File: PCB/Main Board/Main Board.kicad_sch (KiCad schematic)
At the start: 4 parts

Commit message: quality of life changes plus wiring plus buffering plus value changes
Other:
- sheet Auto-Balancing Bridge ports: added AC_100, AC_10k, AC_1k, AC_EN, IBmonitor, OUT+, OUT-, R_SEL_10, R_SEL_100, R_SEL_100k, R_SEL_10k, R_SEL_1k, R_SEL_432k; removed none
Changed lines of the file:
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@@
+	(wire
+		(pts
+			(xy 139.7 133.35) (xy 190.5 133.35)
+		)
+		(stroke
+			(width 0)
+			(type default)
+		)
+	)
+	(wire
+		(pts
+			(xy 139.7 156.21) (xy 190.5 156.21)
+		)
+		(stroke
+			(width 0)
+			(type default)
+		)
+	)
 	(wire
 		(pts
@@
 	(wire
 		(pts
+			(xy 139.7 140.97) (xy 190.5 140.97)
+		)
+		(stroke
+			(width 0)
+			(type default)
+		)
+	)
+	(wire
+		(pts
 			(xy 139.7 78.74) (xy 152.4 78.74)
 		)
@@
 	(wire
 		(pts
+			(xy 139.7 151.13) (xy 190.5 151.13)
+		)
+		(stroke
+			(width 0)
+			(type default)
+		)
+	)
+	(wire
+		(pts
 			(xy 139.7 45.72) (xy 152.4 45.72)
 		)
@@
 	(wire
 		(pts
+			(xy 139.7 130.81) (xy 190.5 130.81)
+		)
+		(stroke
+			(width 0)
+			(type default)
+		)
+	)
+	(wire
+		(pts
+			(xy 139.7 148.59) (xy 190.5 148.59)
+		)
+		(stroke
+			(width 0)
+			(type default)
+		)
+	)
+	(wire
+		(pts
 			(xy 215.9 114.3) (xy 248.92 114.3)
 		)
@@
 	(wire
 		(pts
+			(xy 139.7 153.67) (xy 190.5 153.67)
+		)
+		(stroke
+			(width 0)
+			(type default)
+		)
+	)
+	(wire
+		(pts
 			(xy 139.7 35.56) (xy 152.4 35.56)
 		)
@@
 	(wire
 		(pts
+			(xy 139.7 146.05) (xy 190.5 146.05)
+		)
+		(stroke
+			(width 0)
+			(type default)
+		)
+	)
+	(wire
+		(pts
 			(xy 139.7 86.36) (xy 152.4 86.36)
 		)
@@
 	(wire
 		(pts
+			(xy 139.7 138.43) (xy 190.5 138.43)
+		)
+		(stroke
+			(width 0)
+			(type default)
+		)
+	)
+	(wire
+		(pts
+			(xy 139.7 143.51) (xy 190.5 143.51)
+		)
+		(stroke
+			(width 0)
+			(type default)
+		)
+	)
+	(wire
+		(pts
 			(xy 139.7 114.3) (xy 152.4 114.3)
+		)
+		(stroke
+			(width 0)
+			(type default)
+		)
+	)
+	(wire
+		(pts
+			(xy 139.7 135.89) (xy 190.5 135.89)
 		)
 		(stroke
@@
 	(sheet
 		(at 190.5 101.6)
-		(size 25.4 25.4)
+		(size 25.4 58.42)
 		(exclude_from_sim no)
 		(in_bom yes)
@@
 		)
 		(property "Sheetfile" "Bridge.kicad_sch"
-			(at 190.5 127.5846 0)
+			(at 190.5 160.6046 0)
 			(effects
 				(font
@@
 		(pin "Out-" output
 			(at 190.5 116.84 180)
+			(effects
+				(font
+					(size 1.27 1.27)
+				)
+				(justify left)
+			)
+		)
+		(pin "AC_EN" input
+			(at 190.5 133.35 180)
+			(effects
+				(font
+					(size 1.27 1.27)
+				)
+				(justify left)
+			)
+		)
+		(pin "OUT-" output
+			(at 190.5 119.38 180)
+			(effects
+				(font
+					(size 1.27 1.27)
+				)
+				(justify left)
+			)
+		)
+		(pin "OUT+" output
+			(at 190.5 114.3 180)
+			(effects
+				(font
+					(size 1.27 1.27)
+				)
+				(justify left)
+			)
+		)
+		(pin "AC_100" input
+			(at 190.5 138.43 180)
+			(effects
+				(font
+					(size 1.27 1.27)
+				)
+				(justify left)
+			)
+		)
+		(pin "IBmonitor" output
+			(at 190.5 130.81 180)
+			(effects
+				(font
+					(size 1.27 1.27)
+				)
+				(justify left)
+			)
+		)
+		(pin "AC_1k" input
+			(at 190.5 135.89 180)
+			(effects
+				(font
+					(size 1.27 1.27)
+				)
+				(justify left)
+			)
+		)
+		(pin "AC_10k" input
+			(at 190.5 140.97 180)
+			(effects
+				(font
+					(size 1.27 1.27)
+				)
+				(justify left)
+			)
+		)
+		(pin "R_SEL_100" input
+			(at 190.5 146.05 180)
+			(effects
+				(font
+					(size 1.27 1.27)
+				)
+				(justify left)
+			)
+		)
+		(pin "R_SEL_10" input
+			(at 190.5 143.51 180)
+			(effects
+				(font
+					(size 1.27 1.27)
+				)
+				(justify left)
+			)
+		)
+		(pin "R_SEL_432k" input
+			(at 190.5 156.21 180)
+			(effects
+				(font
+					(size 1.27 1.27)
+				)
+				(justify left)
+			)
+		)
+		(pin "R_SEL_10k" input
+			(at 190.5 148.59 180)
+			(effects
+				(font
+					(size 1.27 1.27)
+				)
+				(justify left)
+			)
+		)
+		(pin "R_SEL_100k" input
+			(at 190.5 153.67 180)
+			(effects
+				(font
+					(size 1.27 1.27)
+				)
+				(justify left)
+			)
+		)
+		(pin "R_SEL_1k" input
+			(at 190.5 151.13 180)
 			(effects
 				(font
@@
 	(sheet
 		(at 114.3 25.4)
-		(size 25.4 101.6)
+		(size 25.4 134.62)
 		(exclude_from_sim no)
 		(in_bom yes)
@@
 		)
 		(property "Sheetfile" "Processor.kicad_sch"
-			(at 114.3 127.5846 0)
-			(effects
-				(font
+			(at 114.3 160.6046 0)
+			(effects
+				(font

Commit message: footprints and minor
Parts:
- gave numbers to parts that had none: 4
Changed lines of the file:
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@@
 		(dnp no)
 		(fields_autoplaced yes)
-		(property "Reference" "J?"
+		(property "Reference" "J4"
 			(at 257.81 113.3231 0)
 			(effects
@@
 			(project "Main Board"
 				(path "/20aae4b7-3fb8-4924-82e8-1e7a29a313f8"
-					(reference "J?")
+					(reference "J4")
 					(unit 1)
 				)
@@
 		(dnp no)
 		(fields_autoplaced yes)
-		(property "Reference" "J?"
+		(property "Reference" "J2"
 			(at 257.81 62.5231 0)
 			(effects
@@
 			(project "Main Board"
 				(path "/20aae4b7-3fb8-4924-82e8-1e7a29a313f8"
-					(reference "J?")
+					(reference "J2")
 					(unit 1)
 				)
@@
 		(dnp no)
 		(fields_autoplaced yes)
-		(property "Reference" "J?"
+		(property "Reference" "J3"
 			(at 257.81 87.9231 0)
 			(effects
@@
 			(project "Main Board"
 				(path "/20aae4b7-3fb8-4924-82e8-1e7a29a313f8"
-					(reference "J?")
+					(reference "J3")
 					(unit 1)
 				)
@@
 		(dnp no)
 		(fields_autoplaced yes)
-		(property "Reference" "J?"
+		(property "Reference" "J1"
 			(at 257.81 37.1231 0)
 			(effects
@@
 			(project ""
 				(path "/20aae4b7-3fb8-4924-82e8-1e7a29a313f8"
-					(reference "J?")
-					(unit 1)
-				)
+					(reference "J1")
+					(unit 1)
+				)

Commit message: footprints and stm wiring
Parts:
- J1, J2, J3, J4: footprint (none) -> Connector_Coaxial:BNC_TEConnectivity_1478035_Horizontal
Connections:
- net Guard_{out} is gone; now on net GUARD: J3.2 (Ext), J4.2 (Ext)
- net GUARD: now reaches J2.2 (Ext)
- net GUARD: now also J1.2 (Ext)
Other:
- sheet Auto-Balancing Bridge ports: added DC_INT_ISO, I_B_MONITOR; removed IBmonitor, Out+, Out-
- sheet Current Amplifier: file Amplifier.kicad_sch -> currentamp.kicad_sch
- sheet Processor ports: added DC_INT_ISO, R_SEL_10, R_SEL_100, R_SEL_10k, R_SEL_1k, SIG_SOURCE; removed none
- sheet Signal Source ports: added SIG_SOURCE; removed none
- sheet Voltage Amplifier: file Amplifier.kicad_sch -> voltageamp.kicad_sch

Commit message: relays and layout begin
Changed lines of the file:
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@@
 	)
 	(sheet
-		(at 77.47 134.62)
+		(at 76.2 135.89)
 		(size 25.4 25.4)
 		(exclude_from_sim no)
@@
 		)
 		(property "Sheetname" "Power"
-			(at 77.47 133.9084 0)
+			(at 76.2 135.1784 0)
 			(effects
 				(font
@@
 		)
 		(property "Sheetfile" "Power.kicad_sch"
-			(at 77.47 160.6046 0)
+			(at 76.2 161.8746 0)
 			(effects
 				(font

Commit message: minor and layout
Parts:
- added H1, H2, H3, H4: MountingHole, MountingHole:MountingHole_3.2mm_M3, symbol Mechanical:MountingHole
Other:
- sheet Auto-Balancing Bridge ports: added none; removed R_SEL_432k
- moved on the sheet: J1, J2, J3, J4

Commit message: :ghost:
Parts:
- renumbered H1 to H101, H2 to H102, H3 to H103, H4 to H104, J1 to J101, J2 to J102, J3 to J103, J4 to J104
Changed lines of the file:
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@@
 		(dnp no)
 		(fields_autoplaced yes)
-		(property "Reference" "H4"
+		(property "Reference" "H104"
 			(at 38.1 149.8599 0)
 			(effects
@@
 			(project "Main Board"
 				(path "/20aae4b7-3fb8-4924-82e8-1e7a29a313f8"
-					(reference "H4")
+					(reference "H104")
 					(unit 1)
 				)
@@
 		(dnp no)
 		(fields_autoplaced yes)
-		(property "Reference" "H3"
+		(property "Reference" "H103"
 			(at 38.1 144.7799 0)
 			(effects
@@
 			(project "Main Board"
 				(path "/20aae4b7-3fb8-4924-82e8-1e7a29a313f8"
-					(reference "H3")
+					(reference "H103")
 					(unit 1)
 				)
@@
 		(dnp no)
 		(fields_autoplaced yes)
-		(property "Reference" "J4"
+		(property "Reference" "J104"
 			(at 233.68 110.7831 0)
 			(effects
@@
 			(project "Main Board"
 				(path "/20aae4b7-3fb8-4924-82e8-1e7a29a313f8"
-					(reference "J4")
+					(reference "J104")
 					(unit 1)
 				)
@@
 		(dnp no)
 		(fields_autoplaced yes)
-		(property "Reference" "J2"
+		(property "Reference" "J102"
 			(at 233.68 59.9831 0)
 			(effects
@@
 			(project "Main Board"
 				(path "/20aae4b7-3fb8-4924-82e8-1e7a29a313f8"
-					(reference "J2")
+					(reference "J102")
 					(unit 1)
 				)
@@
 		(dnp no)
 		(fields_autoplaced yes)
-		(property "Reference" "H2"
+		(property "Reference" "H102"
 			(at 38.1 139.6999 0)
 			(effects
@@
 			(project "Main Board"
 				(path "/20aae4b7-3fb8-4924-82e8-1e7a29a313f8"
-					(reference "H2")
+					(reference "H102")
 					(unit 1)
 				)
@@
 		(dnp no)
 		(fields_autoplaced yes)
-		(property "Reference" "J3"
+		(property "Reference" "J103"
 			(at 233.68 85.3831 0)
 			(effects
@@
 			(project "Main Board"
 				(path "/20aae4b7-3fb8-4924-82e8-1e7a29a313f8"
-					(reference "J3")
+					(reference "J103")
 					(unit 1)
 				)
@@
 		(dnp no)
 		(fields_autoplaced yes)
-		(property "Reference" "H1"
+		(property "Reference" "H101"
 			(at 38.1 134.6199 0)
 			(effects
@@
 			(project ""
 				(path "/20aae4b7-3fb8-4924-82e8-1e7a29a313f8"
-					(reference "H1")
+					(reference "H101")
 					(unit 1)
 				)
@@
 		(dnp no)
 		(fields_autoplaced yes)
-		(property "Reference" "J1"
+		(property "Reference" "J101"
 			(at 233.68 34.5831 0)
 			(effects
@@
 			(project ""
 				(path "/20aae4b7-3fb8-4924-82e8-1e7a29a313f8"
-					(reference "J1")
-					(unit 1)
-				)
+					(reference "J101")
+					(unit 1)
+				)

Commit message: Layout progress
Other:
- sheet Processor ports: added IAmp.Out, VAmp.Out; removed IAmp.In, VAmp.In
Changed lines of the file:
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@@
 			)
 		)
-		(pin "VAmp.In" input
+		(pin "VAmp.Out" input
 			(at 115.57 73.66 0)
 			(effects
@@
 			)
 		)
-		(pin "IAmp.In" input
+		(pin "IAmp.Out" input
 			(at 115.57 111.76 0)
 			(effects

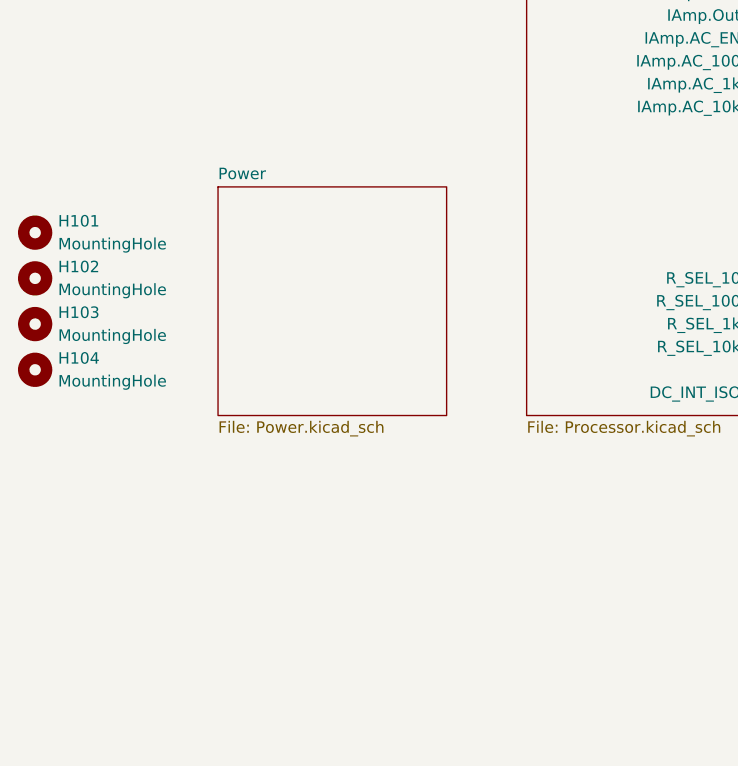
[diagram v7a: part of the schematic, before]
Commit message: transistor tester
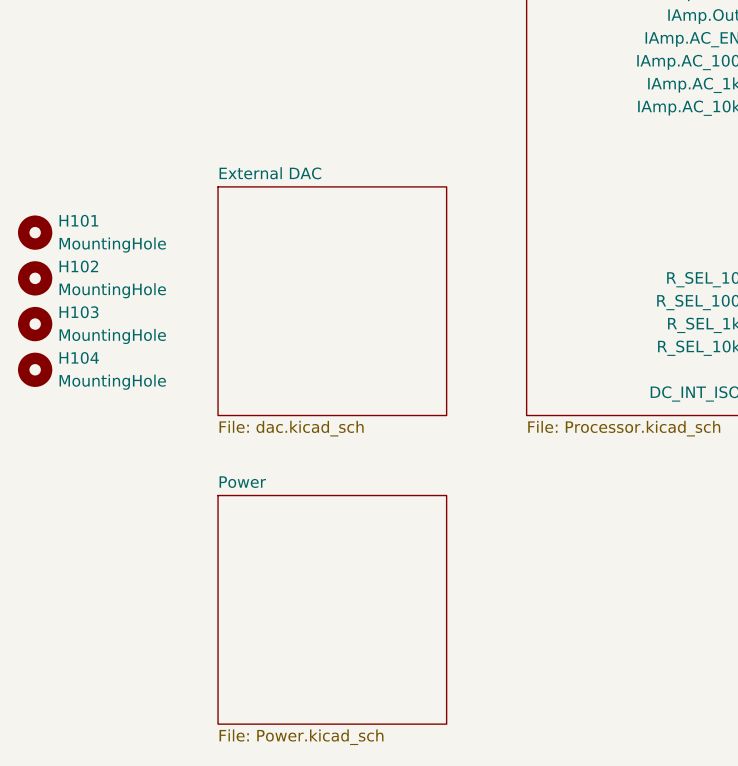
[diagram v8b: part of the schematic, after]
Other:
- added sheet External DAC (dac.kicad_sch)
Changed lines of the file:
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@@
+	)
+	(sheet
+		(at 55.88 165.1)
+		(size 25.4 25.4)
+		(exclude_from_sim no)
+		(in_bom yes)
+		(on_board yes)
+		(dnp no)
+		(fields_autoplaced yes)
+		(stroke
+			(width 0.1524)
+			(type solid)
+		)
+		(fill
+			(color 0 0 0 0.0000)
+		)
+		(property "Sheetname" "Power"
+			(at 55.88 164.3884 0)
+			(effects
+				(font
+					(size 1.27 1.27)
+				)
+				(justify left bottom)
+			)
+		)
+		(property "Sheetfile" "Power.kicad_sch"
+			(at 55.88 191.0846 0)
+			(effects
+				(font
+					(size 1.27 1.27)
+				)
+				(justify left top)
+			)
+		)
+		(instances
+			(project "Main Board"
+				(path "/20aae4b7-3fb8-4924-82e8-1e7a29a313f8"
+					(page "13")
+				)
+			)
+		)
+	)
+	(sheet
+		(at 128.27 99.06)
+		(size 25.4 25.4)
+		(exclude_from_sim no)
+		(in_bom yes)
+		(on_board yes)
+		(dnp no)
+		(fields_autoplaced yes)
+		(stroke
+			(width 0.1524)
+			(type solid)
+		)
+		(fill
+			(color 0 0 0 0.0000)
+		)
+		(property "Sheetname" "Current Amplifier"
+			(at 128.27 98.3484 0)
+			(effects
+				(font
+					(size 1.27 1.27)
+				)
+				(justify left bottom)
+			)
+		)
+		(property "Sheetfile" "currentamp.kicad_sch"
+			(at 128.27 125.0446 0)
+			(effects
+				(font
+					(size 1.27 1.27)
+				)
+				(justify left top)
+			)
+		)
+		(pin "AC_100" input
+			(at 128.27 116.84 180)
+			(effects
+				(font
+					(size 1.27 1.27)
+				)
+				(justify left)
+			)
+		)
+		(pin "AC_EN" input
+			(at 128.27 114.3 180)
+			(effects
+				(font
+					(size 1.27 1.27)
+				)
+				(justify left)
+			)
+		)
+		(pin "x3" input
+			(at 128.27 106.68 180)
+			(effects
+				(font
+					(size 1.27 1.27)
+				)
+				(justify left)
+			)
+		)
+		(pin "{slash}4" input
+			(at 128.27 101.6 180)
+			(effects
+				(font
+					(size 1.27 1.27)
+				)
+				(justify left)
+			)
+		)
+		(pin "In-" input
+			(at 153.67 114.3 0)
+			(effects
+				(font
+					(size 1.27 1.27)
+				)
+				(justify right)
+			)
+		)
+		(pin "AC_1k" input
+			(at 128.27 119.38 180)
+			(effects
+				(font
+					(size 1.27 1.27)
+				)
+				(justify left)
+			)
+		)
+		(pin "~{x100}" input
+			(at 128.27 109.22 180)
+			(effects
+				(font
+					(size 1.27 1.27)
+				)
+				(justify left)
+			)
+		)
+		(pin "In+" input
+			(at 153.67 109.22 0)
+			(effects
+				(font
+					(size 1.27 1.27)
+				)
+				(justify right)
+			)
+		)
+		(pin "AC_10k" input
+			(at 128.27 121.92 180)
+			(effects
+				(font
+					(size 1.27 1.27)
+				)
+				(justify left)
+			)
+		)
+		(pin "Out" output
+			(at 128.27 111.76 180)
+			(effects
+				(font
+					(size 1.27 1.27)
+				)
+				(justify left)
+			)
+		)
+		(pin "x1" input
+			(at 128.27 104.14 180)
+			(effects
+				(font
+					(size 1.27 1.27)
+				)
+				(justify left)
+			)
+		)
+		(instances
+			(project "Main Board"
+				(path "/20aae4b7-3fb8-4924-82e8-1e7a29a313f8"
+					(page "10")
+				)
+			)
+		)
 	)
 	(sheet
@@
 			(color 0 0 0 0.0000)
 		)
-		(property "Sheetname" "Power"
+		(property "Sheetname" "External DAC"
 			(at 55.88 130.0984 0)
 			(effects
@@
 			)
 		)
-		(property "Sheetfile" "Power.kicad_sch"
+		(property "Sheetfile" "dac.kicad_sch"
 			(at 55.88 156.7946 0)
 			(effects
@@
 			(project "Main Board"
 				(path "/20aae4b7-3fb8-4924-82e8-1e7a29a313f8"
-					(page "13")
-				)
-			)
-		)
-	)
-	(sheet
-		(at 128.27 99.06)
-		(size 25.4 25.4)
-		(exclude_from_sim no)
-		(in_bom yes)
-		(on_board yes)
-		(dnp no)
-		(fields_autoplaced yes)
-		(stroke
-			(width 0.1524)
-			(type solid)
-		)
-		(fill
-			(color 0 0 0 0.0000)
-		)
-		(property "Sheetname" "Current Amplifier"
-			(at 128.27 98.3484 0)
-			(effects
-				(font
-					(size 1.27 1.27)
-				)
-				(justify left bottom)
-			)
-		)
-		(property "Sheetfile" "currentamp.kicad_sch"
-			(at 128.27 125.0446 0)
-			(effects
-				(font
-					(size 1.27 1.27)
-				)
-				(justify left top)
-			)
-		)
-		(pin "AC_100" input
-			(at 128.27 116.84 180)
-			(effects
-				(font
-					(size 1.27 1.27)
-				)
-				(justify left)
-			)
-		)
-		(pin "AC_EN" input
-			(at 128.27 114.3 180)
-			(effects
-				(font
-					(size 1.27 1.27)
-				)
-				(justify left)
-			)
-		)
-		(pin "x3" input
-			(at 128.27 106.68 180)
-			(effects
-				(font
-					(size 1.27 1.27)
-				)
-				(justify left)
-			)
-		)
-		(pin "{slash}4" input
-			(at 128.27 101.6 180)
-			(effects
-				(font
-					(size 1.27 1.27)
-				)
-				(justify left)
-			)
-		)
-		(pin "In-" input
-			(at 153.67 114.3 0)
-			(effects
-				(font
-					(size 1.27 1.27)
-				)
-				(justify right)
-			)
-		)
-		(pin "AC_1k" input
-			(at 128.27 119.38 180)
-			(effects
-				(font
-					(size 1.27 1.27)
-				)
-				(justify left)
-			)
-		)
-		(pin "~{x100}" input
-			(at 128.27 109.22 180)
-			(effects
-				(font
-					(size 1.27 1.27)
-				)
-				(justify left)
-			)
-		)
-		(pin "In+" input
-			(at 153.67 109.22 0)
-			(effects
-				(font
-					(size 1.27 1.27)
-				)
-				(justify right)
-			)
-		)
-		(pin "AC_10k" input
-			(at 128.27 121.92 180)
-			(effects
-				(font
-					(size 1.27 1.27)
-				)
-				(justify left)
-			)
-		)
-		(pin "Out" output
-			(at 128.27 111.76 180)
-			(effects
-				(font
-					(size 1.27 1.27)
-				)
-				(justify left)
-			)
-		)
-		(pin "x1" input
-			(at 128.27 104.14 180)
-			(effects
-				(font
-					(size 1.27 1.27)
-				)
-				(justify left)
-			)
-		)
-		(instances
-			(project "Main Board"
-				(path "/20aae4b7-3fb8-4924-82e8-1e7a29a313f8"
-					(page "10")
-				)
-			)
+					(page "9")
+				)
+			)
